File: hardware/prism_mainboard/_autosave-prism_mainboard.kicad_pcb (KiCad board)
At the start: 6 copper layers, 100 x 100 mm, 82 parts, among them IC1 KTDM4G3C618BGIEAT, IC2 KTDM4G3C618BGIEAT, IC3 USB3320C-EZK, J1 503398-1892, J2 UJ32-21-C-H-G-HMT-LT-P24-TR, U1 XC7Z015-2CLG485I, U2 LMS7002M, U3 PEC16-4220F-S0024, U4 AMS1117-1.8, U5 AMS1117-1.8, U6 AMS1117-1.8, U7 AMS1117-1.8

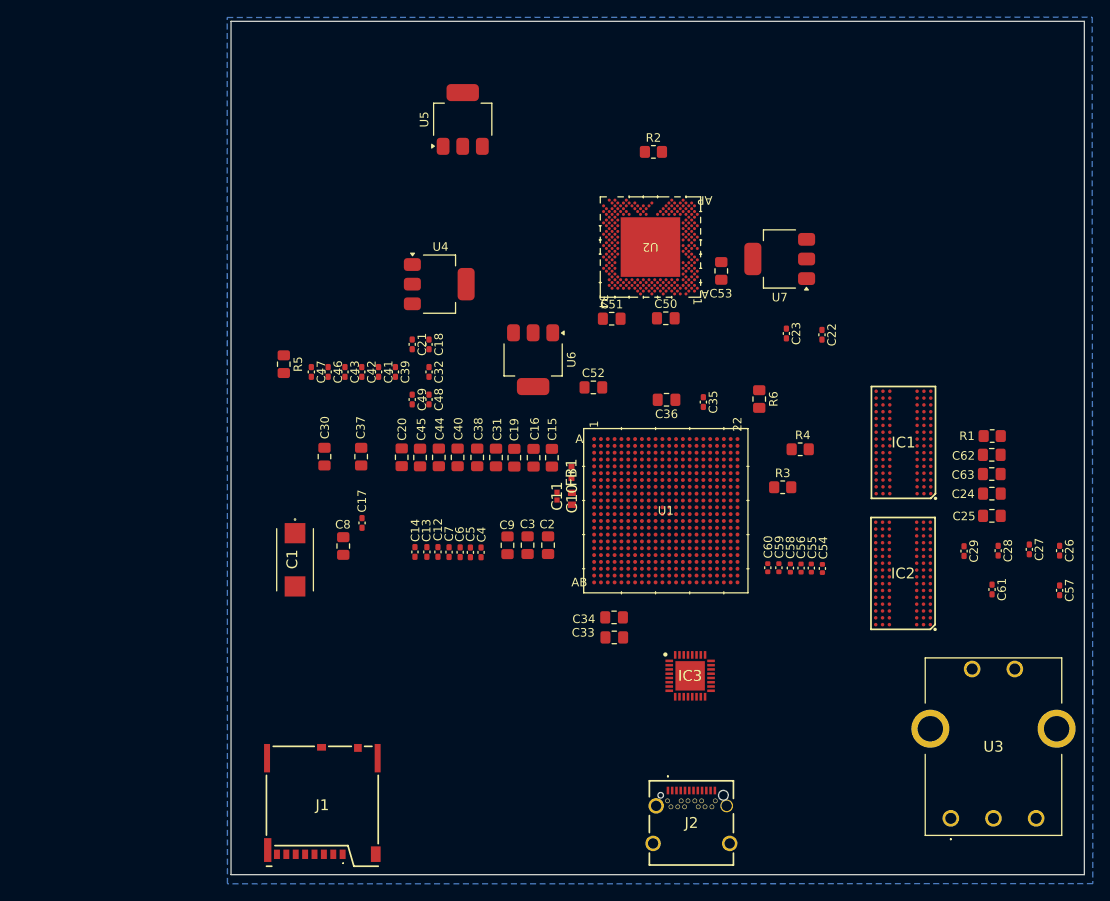
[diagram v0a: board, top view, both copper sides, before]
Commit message: Layout Update and References
Small layout updates, and added some SDR references to see what I can take from them.
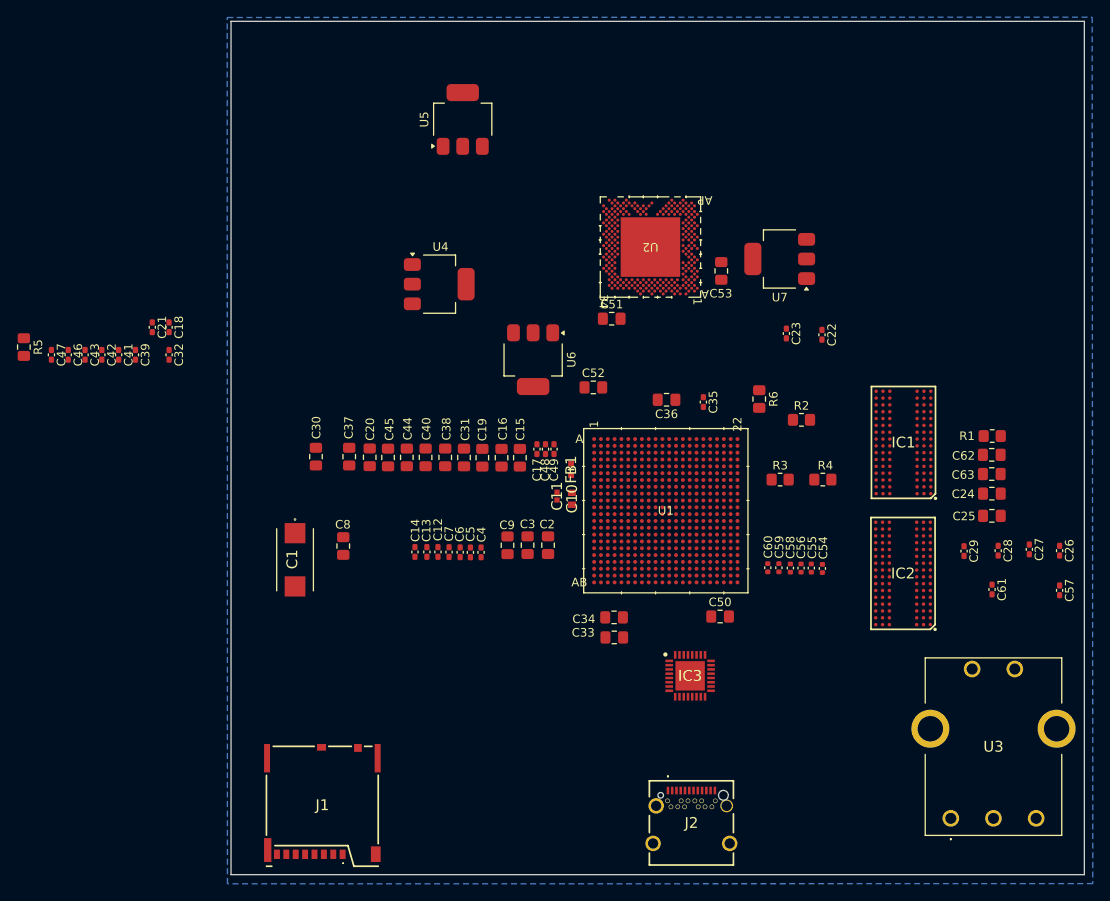
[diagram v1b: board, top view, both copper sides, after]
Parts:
- moved R2 35.9 mm to (144.5, 103.5)
- moved C50 35.5 mm to (135.0, 126.5)
- moved C42 30.5 mm to (62.5, 95.9)
- moved C43 30.5 mm to (60.5, 95.9)
- moved C46 30.5 mm to (58.6, 95.9)
- moved C47 30.5 mm to (56.6, 95.9)
- moved R5 30.5 mm to (53.4, 95.0)
- moved C18 30.5 mm to (70.4, 92.7)
- moved C21 30.5 mm to (68.4, 92.7)
- moved C32 30.5 mm to (70.4, 95.9)
- moved C39 30.5 mm to (66.5, 95.9)
- moved C41 30.5 mm to (64.5, 95.9)
- moved C17 22.3 mm to (113.5, 106.9), turned to 90 degrees
- moved C49 17.6 mm to (115.5, 106.9), turned to 90 degrees
- moved C48 14.8 mm to (114.5, 106.9), turned to 90 degrees
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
